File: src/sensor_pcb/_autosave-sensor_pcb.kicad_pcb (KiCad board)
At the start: 2 copper layers, 64 x 64 mm, 78 parts, among them IC1 TCAN3414DRBR, J1 66200421024, J2 643280100305, J3 66200821024, J4 643280100305, J5 66200821024, J7 66200421024, Q1 NPN BJT 40V 200mA, Q2 NPN BJT 40V 200mA, Q3 NPN BJT 40V 200mA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

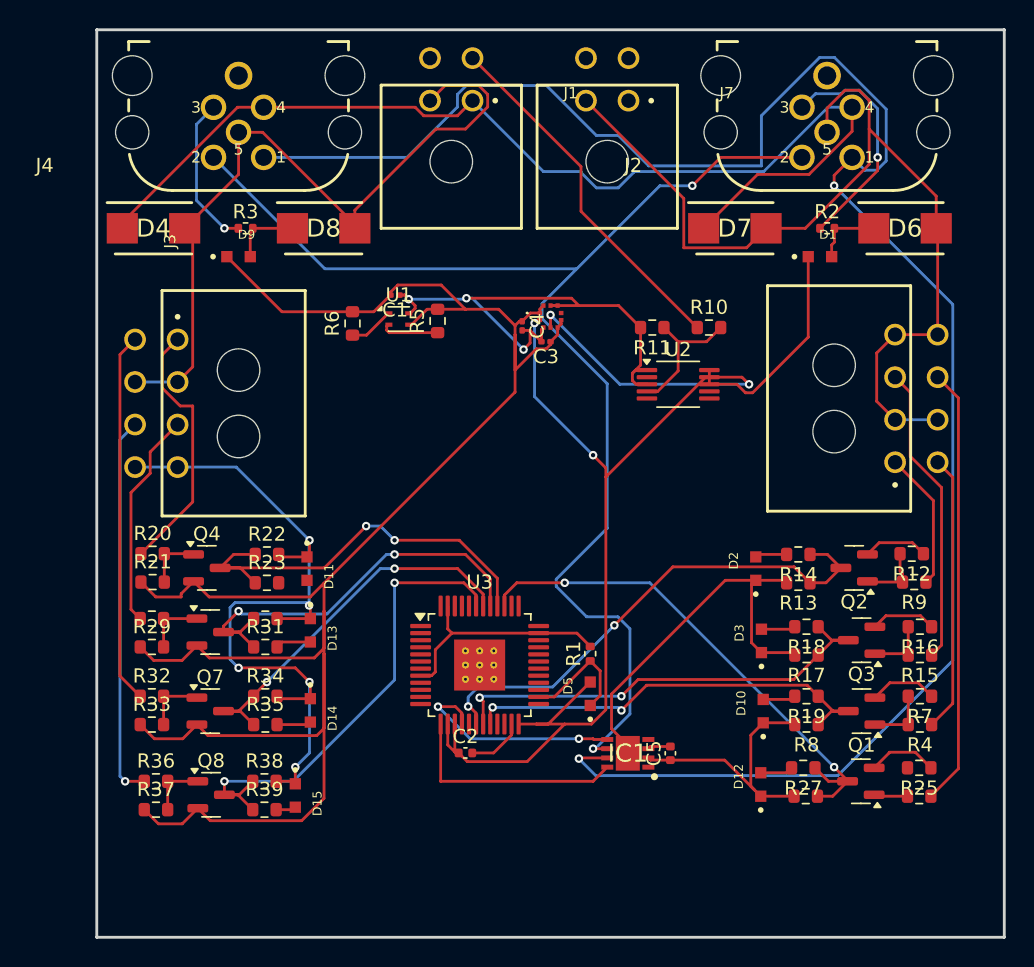
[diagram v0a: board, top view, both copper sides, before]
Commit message: fixing up parts according to kicad auto errors
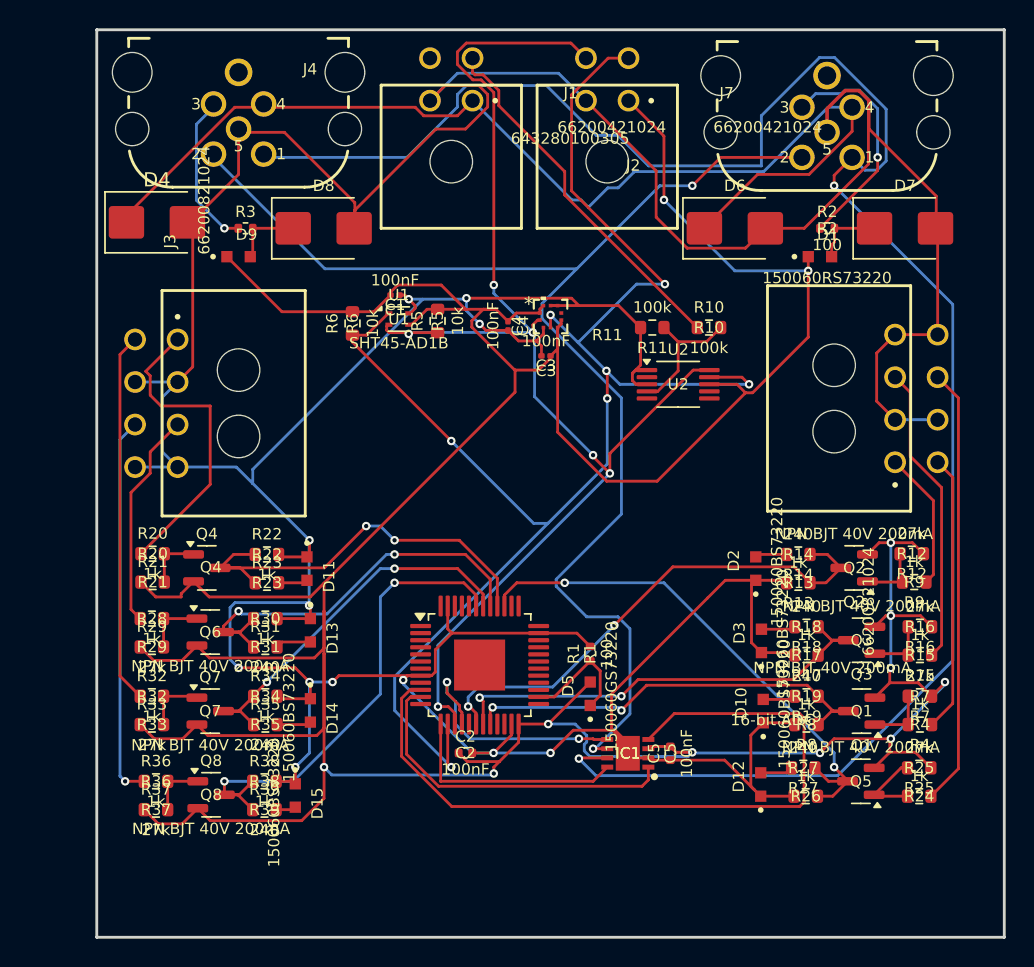
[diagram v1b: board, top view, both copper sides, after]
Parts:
- D4, D6, D7, D8: value SMBJ33A -> SMBJ3.3A; footprint dz_dio:DIOM5436X244N -> Diode_SMD:D_SMB
- U3: footprint Package_QFP:LQFP-48-1EP_7x7mm_P0.5mm_EP3.6x3.6mm_ThermalVias -> dz_mcu:STM32L451CET6
- U4: footprint dz_sens:BMP581 -> dz_sens:QFN10_BMP581_BOS
- moved D6 12.0 mm to (183.0, 69.0)
- moved D7 12.0 mm to (195.0, 69.0)
- moved C3 1.00 mm to (169.7, 78.0)
- moved C4 1.00 mm to (167.0, 75.9)
- moved D4 0.48 mm to (142.2, 68.6)
- moved J4 0.23 mm to (148.0, 62.0)
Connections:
- D1 pad A: Net-(D6-K) -> Net-(D7-A1)
- D4 pad 1: /5V -> +5V
- D6 pad 1: Net-(D6-K) -> +5V
- D7 pad 1: /5V -> Net-(D7-A1)
- J1 pad 1: /5V -> +5V
- J2 pad 4: /5V -> +5V
- J4 pad 4: /5V -> +5V
- R2 pad 2: Net-(D6-K) -> Net-(D7-A1)
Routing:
- net /VDD: track 178.7 -> 296.6 mm, vias 0 -> 12
- net /SDA: track 22.7 -> 110.2 mm, vias 2 -> 7
- net +5V: track 0.00 -> 77.1 mm
- net /5V: track 75.9 -> 0.00 mm
- net GND: track 281.9 -> 357.6 mm, vias 8 -> 12
- net /CAN_RX: track 0.00 -> 53.4 mm
- net /CAN_TX: track 0.00 -> 23.9 mm
- net /SCL: track 69.9 -> 92.9 mm, vias 2 -> 6
- net Net-(D7-A1): track 0.00 -> 4.86 mm
- net Net-(D6-K): track 4.86 -> 0.00 mm
- net /ls 5.1: track 18.5 -> 22.0 mm
- net Net-(Q5-B): track 2.39 -> 5.53 mm
- net /SHDN: track 15.5 -> 17.8 mm
- net Net-(D11-PadA): track 0.00 -> 2.07 mm
- net /CAN_L: track 91.9 -> 92.7 mm
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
